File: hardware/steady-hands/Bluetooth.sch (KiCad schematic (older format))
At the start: 2 parts

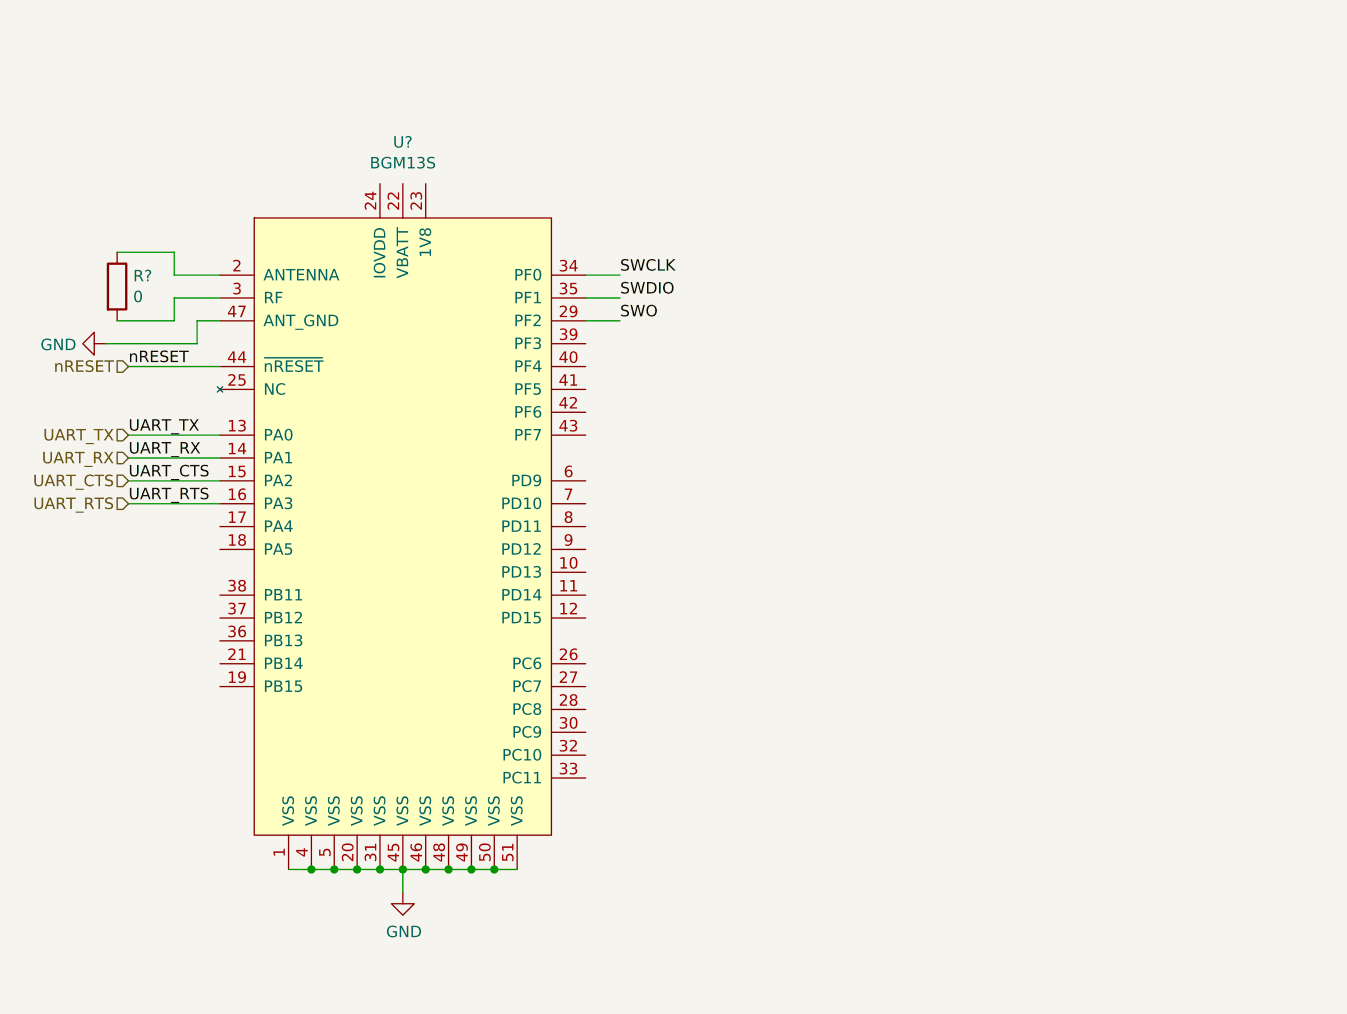
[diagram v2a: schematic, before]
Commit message: Completes schematic connections
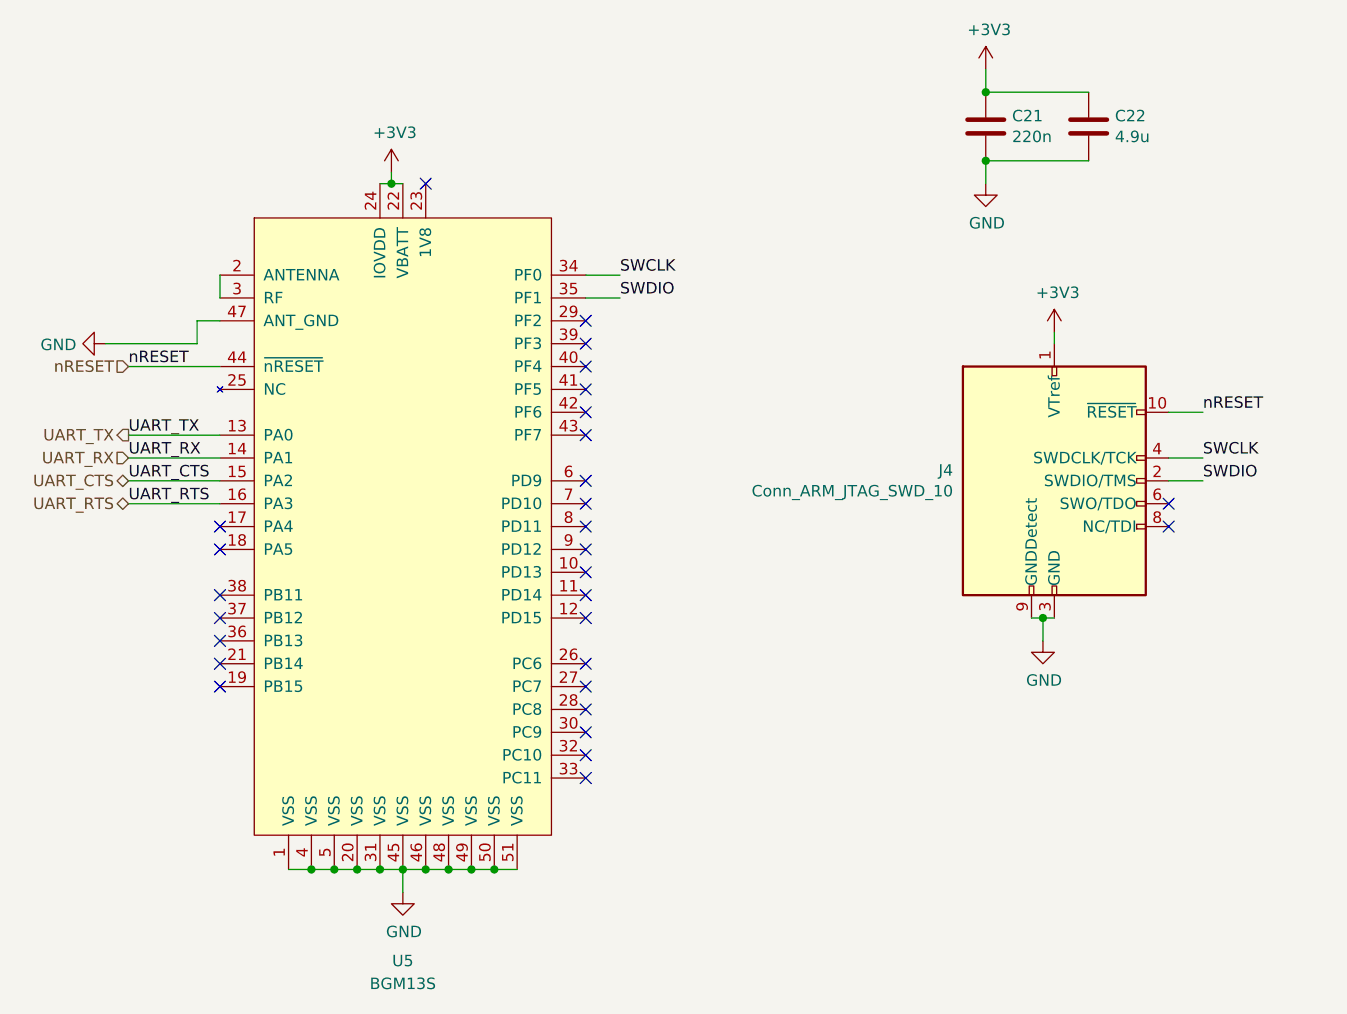
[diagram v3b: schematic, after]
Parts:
- removed R?: 0, symbol Device:R
- added C21: 220n, symbol Device:C
- added C22: 4.9u, symbol Device:C
- added J4: Conn_ARM_JTAG_SWD_10, symbol Connector:Conn_ARM_JTAG_SWD_10
- gave numbers to parts that had none: 1
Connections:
- net GND: now also C21.2, C22.2, J4.3 (GND), J4.5 (GND), J4.9 (GNDDetect)
- net SWCLK: now also J4.4 (SWDCLK/TCK)
- net SWDIO: now also J4.2 (SWDIO/TMS)
- net nRESET: now also J4.10 (~RESET~)
- net at U5.2 (ANTENNA): now also U5.3 (RF)
- net +3V3: now reaches U5.22 (VBATT)
- net +3V3: now also U5.24 (IOVDD), C21.1, C22.1, J4.1 (VTref)
- net SWO: no longer names the net of U5.29 (PF2)
- no-connect marks 0 -> 29
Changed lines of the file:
@@
 P 5800 3650
 AR Path="/5EF78FC7" Ref="U?"  Part="1"
-AR Path="/5EF722F6/5EF78FC7" Ref="U?"  Part="1"
-F 0 "U?" H 5800 5431 50  0000 C CNN
-F 1 "BGM13S" H 5800 5340 50  0000 C CNN
+AR Path="/5EF722F6/5EF78FC7" Ref="U5"  Part="1"
+F 0 "U5" H 5800 1850 50  0000 C CNN
+F 1 "BGM13S" H 5800 1750 50  0000 C CNN
 F 2 "Sij_MCU:BGM13S" H 5800 3800 50  0001 C CNN
 F 3 "https://www.silabs.com/documents/login/data-sheets/bgm13s-datasheet.pdf" H 5800 3800 50  0001 C CNN
@@
 Text Label 4600 2850 0    50   ~ 0
 nRESET
-Wire Wire Line
-	6600 2650 6750 2650
-Text Label 6750 2650 0    50   ~ 0
-SWO
-Text HLabel 4600 3150 0    50   Input ~ 0
+Text HLabel 4600 3150 0    50   Output ~ 0
 UART_TX
 Text HLabel 4600 3250 0    50   Input ~ 0
 UART_RX
-Text HLabel 4600 3350 0    50   Input ~ 0
+Text HLabel 4600 3350 0    50   BiDi ~ 0
 UART_CTS
-Text HLabel 4600 3450 0    50   Input ~ 0
+Text HLabel 4600 3450 0    50   BiDi ~ 0
 UART_RTS
 Text HLabel 4600 2850 0    50   Input ~ 0
 nRESET
-$Comp
-L Device:R R?
-U 1 1 5EFC018D
-P 4550 2500
-F 0 "R?" H 4620 2546 50  0000 L CNN
-F 1 "0" H 4620 2455 50  0000 L CNN
-F 2 "" V 4480 2500 50  0001 C CNN
-F 3 "~" H 4550 2500 50  0001 C CNN
-	1    4550 2500
-	1    0    0    -1
-$EndComp
-Wire Wire Line
-	5000 2450 4800 2450
-Wire Wire Line
-	4800 2450 4800 2350
-Wire Wire Line
-	4800 2350 4550 2350
-Wire Wire Line
-	5000 2550 4800 2550
-Wire Wire Line
-	4800 2550 4800 2650
-Wire Wire Line
-	4800 2650 4550 2650
 Wire Wire Line
 	5000 2650 4900 2650
@@
 	4900 2750 4500 2750
 $Comp
-L power:GND #PWR?
+L power:GND #PWR0137
 U 1 1 5EFC41D5
 P 4500 2750
-F 0 "#PWR?" H 4500 2500 50  0001 C CNN
+F 0 "#PWR0137" H 4500 2500 50  0001 C CNN
 F 1 "GND" V 4505 2622 50  0000 R CNN
 F 2 "" H 4500 2750 50  0001 C CNN
@@
 	5800 5050 5800 5150
 $Comp
-L power:GND #PWR?
+L power:GND #PWR0138
 U 1 1 5EFC4D28
 P 5800 5150
-F 0 "#PWR?" H 5800 4900 50  0001 C CNN
+F 0 "#PWR0138" H 5800 4900 50  0001 C CNN
 F 1 "GND" H 5805 4977 50  0000 C CNN
 F 2 "" H 5800 5150 50  0001 C CNN
@@
 	1    0    0    -1
 $EndComp
+$Comp
+L Connector:Conn_ARM_JTAG_SWD_10 J4
+U 1 1 5F142B1F
+P 8650 3350
+F 0 "J4" H 8207 3396 50  0000 R CNN
+F 1 "Conn_ARM_JTAG_SWD_10" H 8207 3305 50  0000 R CNN
+F 2 "" H 8650 3350 50  0001 C CNN
+F 3 "http://infocenter.arm.com/help/topic/com.arm.doc.ddi0314h/DDI0314H_coresight_components_trm.pdf" V 8300 2100 50  0001 C CNN
+	1    8650 3350
+	1    0    0    -1
+$EndComp
+Wire Wire Line
+	9150 3250 9300 3250
+Text Label 9300 3250 0    50   ~ 0
+SWCLK
+Text Label 9300 3350 0    50   ~ 0
+SWDIO
+Wire Wire Line
+	9300 3350 9150 3350
+Wire Wire Line
+	8650 2750 8650 2700
+Wire Wire Line
+	9150 3050 9300 3050
+Text Label 9300 3050 0    50   ~ 0
+nRESET
+NoConn ~ 9150 3550
+NoConn ~ 9150 3450
+$Comp
+L power:+3V3 #PWR0139
+U 1 1 5F1483CA
+P 8650 2700
+F 0 "#PWR0139" H 8650 2550 50  0001 C CNN
+F 1 "+3V3" H 8665 2873 50  0000 C CNN
+F 2 "" H 8650 2700 50  0001 C CNN
+F 3 "" H 8650 2700 50  0001 C CNN
+	1    8650 2700
+	1    0    0    -1
+$EndComp
+$Comp
+L power:GND #PWR0140
+U 1 1 5F14849D
+P 8600 4050
+F 0 "#PWR0140" H 8600 3800 50  0001 C CNN
+F 1 "GND" H 8605 3877 50  0000 C CNN
+F 2 "" H 8600 4050 50  0001 C CNN
+F 3 "" H 8600 4050 50  0001 C CNN
+	1    8600 4050
+	1    0    0    -1
+$EndComp
+Wire Wire Line
+	8650 3950 8600 3950
+Wire Wire Line
+	8600 3950 8600 4050
+Connection ~ 8600 3950
+Wire Wire Line
+	8600 3950 8550 3950
+NoConn ~ 6600 2650
+NoConn ~ 6600 2750
+NoConn ~ 6600 2850
+NoConn ~ 6600 2950
+NoConn ~ 6600 3050
+NoConn ~ 6600 3150
+NoConn ~ 6600 3350
+NoConn ~ 6600 3450
+NoConn ~ 6600 3550
+NoConn ~ 6600 3650
+NoConn ~ 6600 3750
+NoConn ~ 6600 3850
+NoConn ~ 6600 3950
+NoConn ~ 6600 4150
+NoConn ~ 6600 4250
+NoConn ~ 6600 4350
+NoConn ~ 6600 4450
+NoConn ~ 6600 4550
+NoConn ~ 6600 4650
+NoConn ~ 5000 3550
+NoConn ~ 5000 3650
+NoConn ~ 5000 3850
+NoConn ~ 5000 3950
+NoConn ~ 5000 4050
+NoConn ~ 5000 4150
+NoConn ~ 5000 4250
+Wire Wire Line
+	5700 2050 5750 2050
+Wire Wire Line
+	5750 2050 5750 2000
+Connection ~ 5750 2050
+Wire Wire Line
+	5750 2050 5800 2050
+$Comp
+L power:+3V3 #PWR0141
+U 1 1 5F155003
+P 5750 2000
+F 0 "#PWR0141" H 5750 1850 50  0001 C CNN
+F 1 "+3V3" H 5765 2173 50  0000 C CNN
+F 2 "" H 5750 2000 50  0001 C CNN
+F 3 "" H 5750 2000 50  0001 C CNN
+	1    5750 2000
+	1    0    0    -1
+$EndComp
+NoConn ~ 5900 2050
+$Comp
+L Device:C C21
+U 1 1 5F156DBD
+P 8350 1800
+F 0 "C21" H 8465 1846 50  0000 L CNN
+F 1 "220n" H 8465 1755 50  0000 L CNN
+F 2 "" H 8388 1650 50  0001 C CNN
+F 3 "~" H 8350 1800 50  0001 C CNN
+	1    8350 1800
+	1    0    0    -1
+$EndComp
+$Comp
+L Device:C C22
+U 1 1 5F1574B3
+P 8800 1800
+F 0 "C22" H 8915 1846 50  0000 L CNN
+F 1 "4.9u" H 8915 1755 50  0000 L CNN
+F 2 "" H 8838 1650 50  0001 C CNN
+F 3 "~" H 8800 1800 50  0001 C CNN
+	1    8800 1800
+	1    0    0    -1
+$EndComp
+Wire Wire Line
+	8800 1650 8350 1650
+Wire Wire Line
+	8800 1950 8350 1950
+Connection ~ 8350 1650
+Wire Wire Line
+	8350 1550 8350 1650
+Wire Wire Line
+	8350 1950 8350 2050
+Connection ~ 8350 1950
+$Comp
+L power:+3V3 #PWR0142
+U 1 1 5F15A77D
+P 8350 1550
+F 0 "#PWR0142" H 8350 1400 50  0001 C CNN
+F 1 "+3V3" H 8365 1723 50  0000 C CNN
+F 2 "" H 8350 1550 50  0001 C CNN
+F 3 "" H 8350 1550 50  0001 C CNN
+	1    8350 1550
+	1    0    0    -1
+$EndComp
+$Comp
+L power:GND #PWR0143
+U 1 1 5F15AB86
+P 8350 2050
+F 0 "#PWR0143" H 8350 1800 50  0001 C CNN
+F 1 "GND" H 8355 1877 50  0000 C CNN
+F 2 "" H 8350 2050 50  0001 C CNN
+F 3 "" H 8350 2050 50  0001 C CNN
+	1    8350 2050
+	1    0    0    -1
+$EndComp
+Wire Wire Line
+	5000 2450 5000 2550
 $EndSCHEMATC

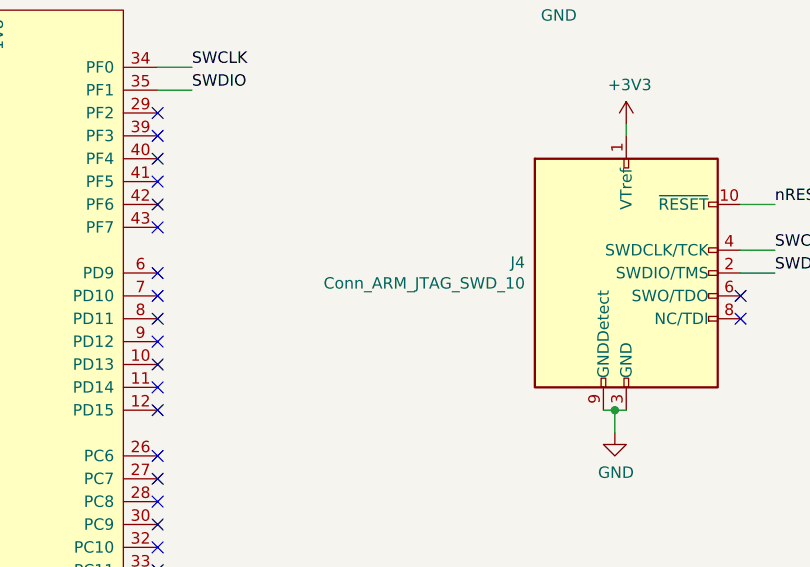
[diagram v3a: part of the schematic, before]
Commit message: Edits label names and switch configuration
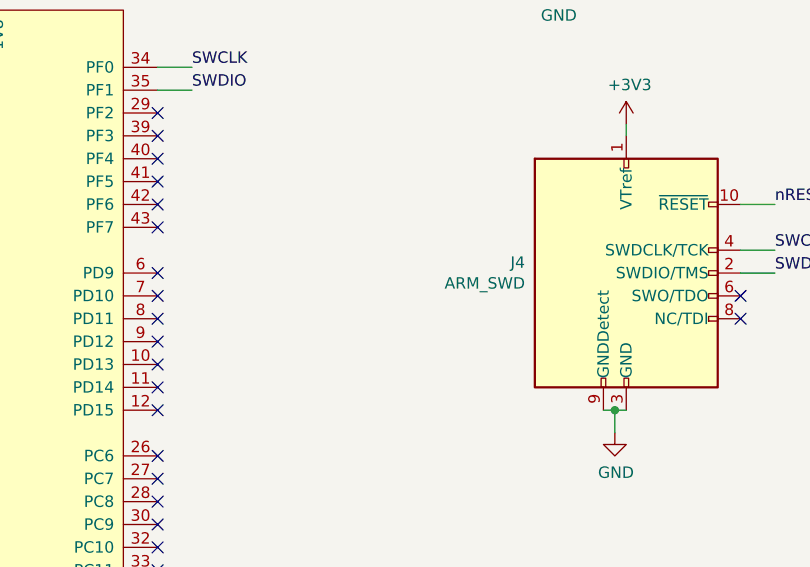
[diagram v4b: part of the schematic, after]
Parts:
- J4: value Conn_ARM_JTAG_SWD_10 -> ARM_SWD
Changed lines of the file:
@@
 $Descr A4 11693 8268
 encoding utf-8
-Sheet 6 7
+Sheet 7 7
 Title ""
 Date ""
@@
 P 8650 3350
 F 0 "J4" H 8207 3396 50  0000 R CNN
-F 1 "Conn_ARM_JTAG_SWD_10" H 8207 3305 50  0000 R CNN
+F 1 "ARM_SWD" H 8207 3305 50  0000 R CNN
 F 2 "" H 8650 3350 50  0001 C CNN
 F 3 "http://infocenter.arm.com/help/topic/com.arm.doc.ddi0314h/DDI0314H_coresight_components_trm.pdf" V 8300 2100 50  0001 C CNN

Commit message: Adds footprints
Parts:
- C21, C22: footprint (none) -> Capacitor_SMD:C_0402_1005Metric
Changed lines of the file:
@@
 $Descr A4 11693 8268
 encoding utf-8
-Sheet 7 7
+Sheet 6 6
 Title ""
 Date ""
@@
 F 0 "C21" H 8465 1846 50  0000 L CNN
 F 1 "220n" H 8465 1755 50  0000 L CNN
-F 2 "" H 8388 1650 50  0001 C CNN
+F 2 "Capacitor_SMD:C_0402_1005Metric" H 8388 1650 50  0001 C CNN
 F 3 "~" H 8350 1800 50  0001 C CNN
 	1    8350 1800
@@
 F 0 "C22" H 8915 1846 50  0000 L CNN
 F 1 "4.9u" H 8915 1755 50  0000 L CNN
-F 2 "" H 8838 1650 50  0001 C CNN
+F 2 "Capacitor_SMD:C_0402_1005Metric" H 8838 1650 50  0001 C CNN
 F 3 "~" H 8800 1800 50  0001 C CNN
 	1    8800 1800

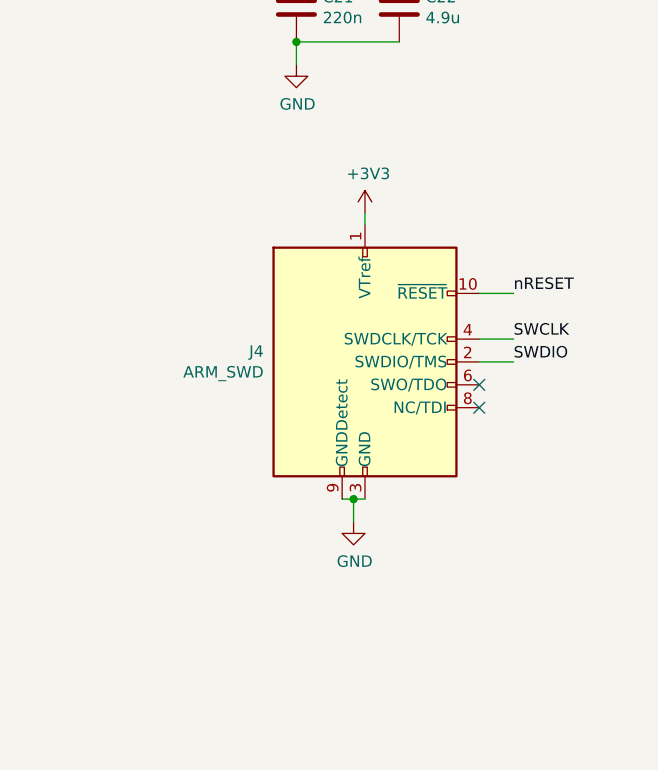
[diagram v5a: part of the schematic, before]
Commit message: Adds all footprints to board
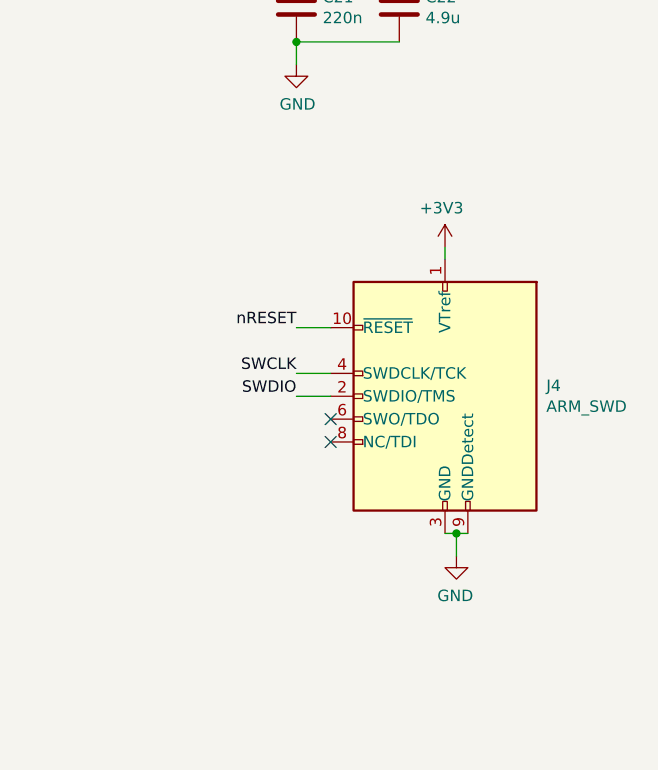
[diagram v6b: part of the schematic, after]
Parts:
- J4: footprint (none) -> Sij_Connectors:FTSH-105-01-X-DV
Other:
- moved on the sheet: J4
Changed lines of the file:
@@
 L Connector:Conn_ARM_JTAG_SWD_10 J4
 U 1 1 5F142B1F
-P 8650 3350
-F 0 "J4" H 8207 3396 50  0000 R CNN
-F 1 "ARM_SWD" H 8207 3305 50  0000 R CNN
-F 2 "" H 8650 3350 50  0001 C CNN
-F 3 "http://infocenter.arm.com/help/topic/com.arm.doc.ddi0314h/DDI0314H_coresight_components_trm.pdf" V 8300 2100 50  0001 C CNN
-	1    8650 3350
-	1    0    0    -1
+P 9000 3500
+F 0 "J4" H 8557 3546 50  0000 R CNN
+F 1 "ARM_SWD" H 8557 3455 50  0000 R CNN
+F 2 "Sij_Connectors:FTSH-105-01-X-DV" H 9000 3500 50  0001 C CNN
+F 3 "http://infocenter.arm.com/help/topic/com.arm.doc.ddi0314h/DDI0314H_coresight_components_trm.pdf" V 8650 2250 50  0001 C CNN
+	1    9000 3500
+	-1   0    0    -1
 $EndComp
 Wire Wire Line
-	9150 3250 9300 3250
-Text Label 9300 3250 0    50   ~ 0
+	8500 3400 8350 3400
+Text Label 8350 3400 2    50   ~ 0
 SWCLK
-Text Label 9300 3350 0    50   ~ 0
+Text Label 8350 3500 2    50   ~ 0
 SWDIO
 Wire Wire Line
-	9300 3350 9150 3350
+	8350 3500 8500 3500
 Wire Wire Line
-	8650 2750 8650 2700
+	9000 2900 9000 2850
 Wire Wire Line
-	9150 3050 9300 3050
-Text Label 9300 3050 0    50   ~ 0
+	8500 3200 8350 3200
+Text Label 8350 3200 2    50   ~ 0
 nRESET
-NoConn ~ 9150 3550
-NoConn ~ 9150 3450
+NoConn ~ 8500 3700
+NoConn ~ 8500 3600
 $Comp
 L power:+3V3 #PWR0139
 U 1 1 5F1483CA
-P 8650 2700
-F 0 "#PWR0139" H 8650 2550 50  0001 C CNN
-F 1 "+3V3" H 8665 2873 50  0000 C CNN
-F 2 "" H 8650 2700 50  0001 C CNN
-F 3 "" H 8650 2700 50  0001 C CNN
-	1    8650 2700
-	1    0    0    -1
+P 9000 2850
+F 0 "#PWR0139" H 9000 2700 50  0001 C CNN
+F 1 "+3V3" H 9015 3023 50  0000 C CNN
+F 2 "" H 9000 2850 50  0001 C CNN
+F 3 "" H 9000 2850 50  0001 C CNN
+	1    9000 2850
+	-1   0    0    -1
 $EndComp
 $Comp
 L power:GND #PWR0140
 U 1 1 5F14849D
-P 8600 4050
-F 0 "#PWR0140" H 8600 3800 50  0001 C CNN
-F 1 "GND" H 8605 3877 50  0000 C CNN
-F 2 "" H 8600 4050 50  0001 C CNN
-F 3 "" H 8600 4050 50  0001 C CNN
-	1    8600 4050
-	1    0    0    -1
+P 9050 4200
+F 0 "#PWR0140" H 9050 3950 50  0001 C CNN
+F 1 "GND" H 9055 4027 50  0000 C CNN
+F 2 "" H 9050 4200 50  0001 C CNN
+F 3 "" H 9050 4200 50  0001 C CNN
+	1    9050 4200
+	-1   0    0    -1
 $EndComp
 Wire Wire Line
-	8650 3950 8600 3950
+	9000 4100 9050 4100
 Wire Wire Line
-	8600 3950 8600 4050
-Connection ~ 8600 3950
+	9050 4100 9050 4200
+Connection ~ 9050 4100
 Wire Wire Line
-	8600 3950 8550 3950
+	9050 4100 9100 4100
 NoConn ~ 6600 2650
 NoConn ~ 6600 2750
